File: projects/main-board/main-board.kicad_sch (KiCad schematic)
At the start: 0 parts

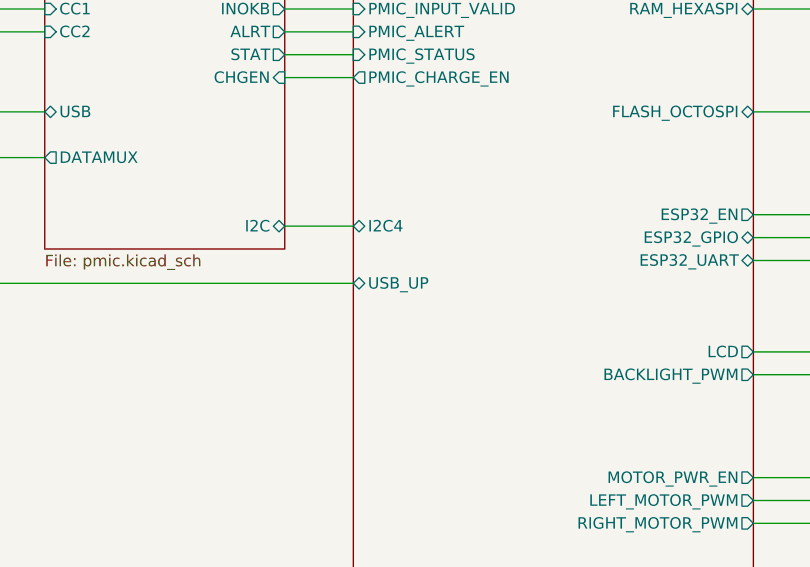
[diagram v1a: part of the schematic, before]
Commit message: Main board PCB layout and routing
- Add 48MHz crystal for STM32
- Add 32kHz crystal for STM32
- Started laying out and routing board
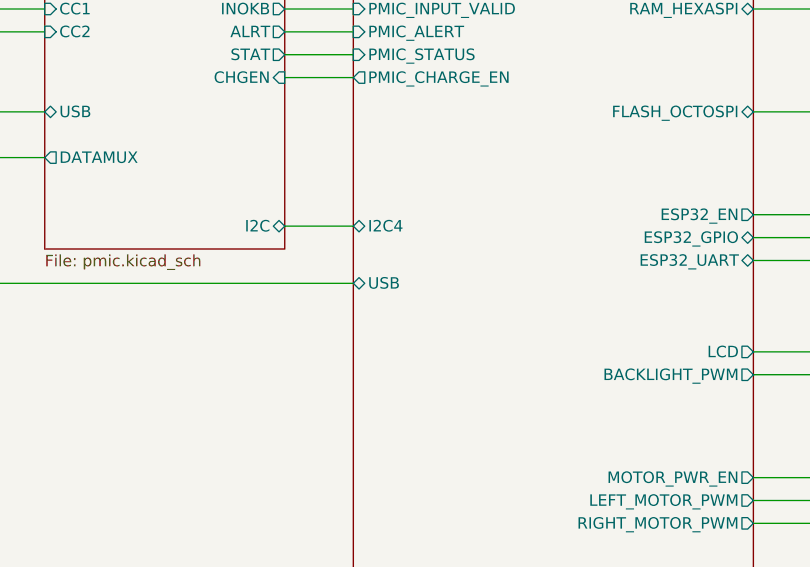
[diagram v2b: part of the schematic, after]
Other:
- sheet MCU ports: added USB; removed USB_UP
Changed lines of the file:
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@@
 			)
 		)
-		(pin "USB_UP" bidirectional
+		(pin "USB" bidirectional
 			(at 146.05 73.66 180)
 			(effects

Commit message: WIP splitting main board into 3
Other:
- removed sheet Buttons
- added sheet Controllers (controllers.kicad_sch)
- sheet Audio ports: added LEFT_SPEAKER, RIGHT_SPEAKER; removed none
- sheet Haptics ports: added LEFT_MOTOR, RIGHT_MOTOR; removed none
